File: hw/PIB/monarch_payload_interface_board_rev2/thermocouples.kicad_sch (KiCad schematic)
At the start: 30 parts, among them U3 MAX31856MUD_T, U5 MAX31856MUD_T, U6 MAX31856MUD_T, U7 MAX31856MUD_T, U8 MAX31856MUD_T

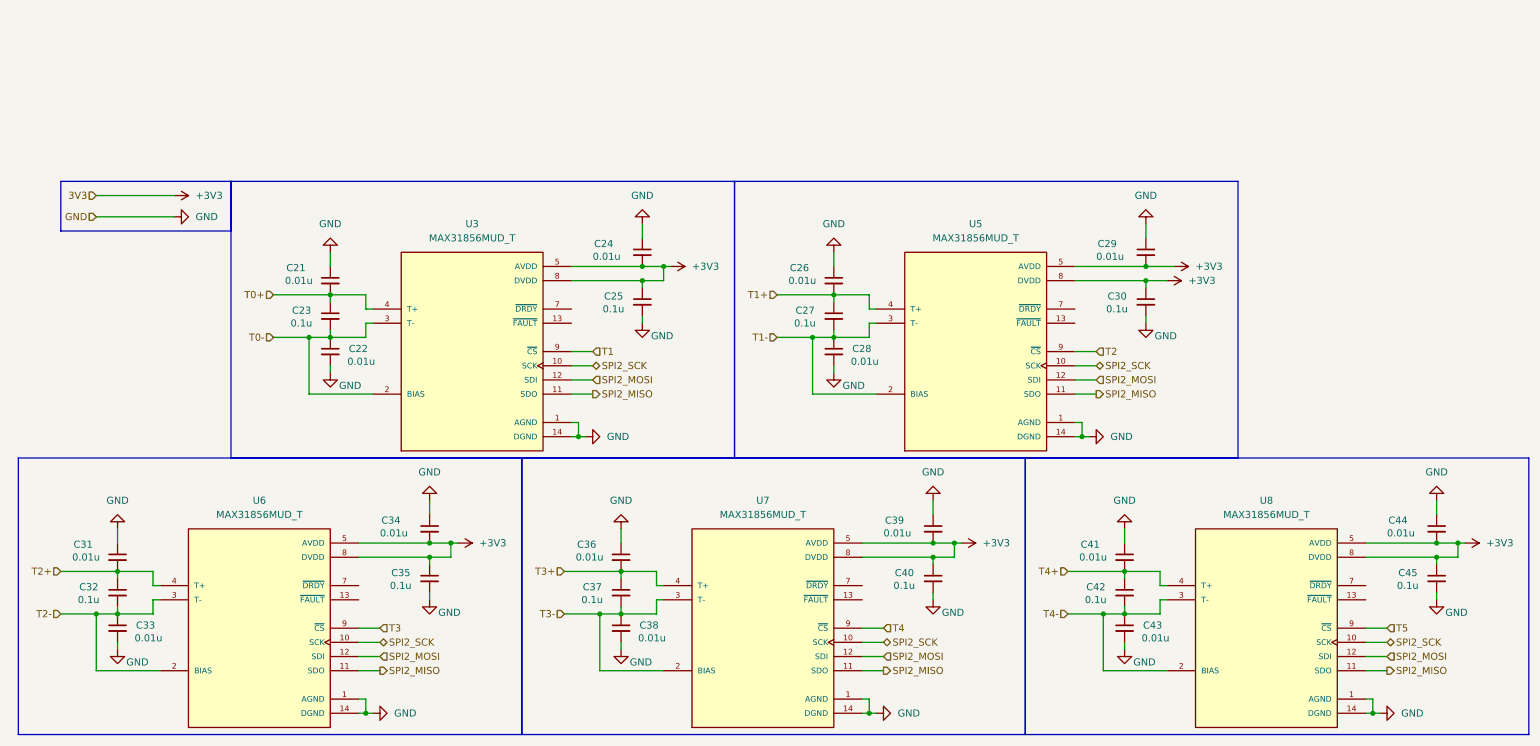
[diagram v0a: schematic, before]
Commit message: MCU Power Pins Fix
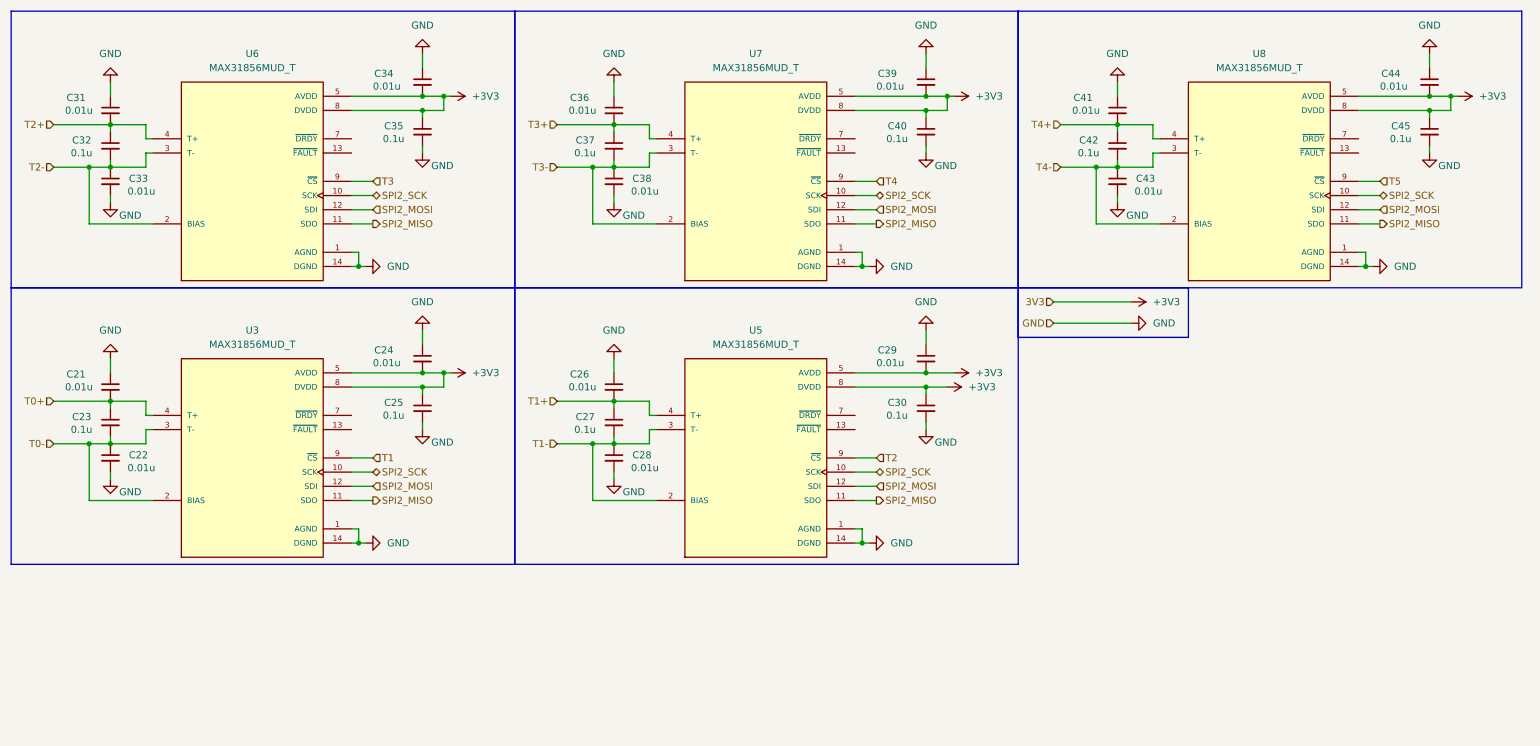
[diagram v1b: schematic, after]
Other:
- moved on the sheet: C21, C22, C23, C24, C25, C26, C27, C28, C29, C30, C31, C32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
